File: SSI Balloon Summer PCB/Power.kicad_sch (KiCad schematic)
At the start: 36 parts, among them J1 Battery connector, Q2 DMG2305UX-7, SW1 SW_SPDT, U2 TPS63070RNMR, U3 AP2112K-3.3TRG1, U6 TPS63070RNMR

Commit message: finished footprints for PWR sheet
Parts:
- added D2: BZT52C5V1, Diode_SMD:D_SOD-123, symbol Device:D_Zener
- C1, C10, C19, C9: footprint (none) -> Capacitor_SMD:C_0603_1608Metric
- C15, C16, C17, C18, C2, C20, C21, C22, C3, C4, C5, C6, C7, C8: footprint (none) -> Capacitor_SMD:C_0805_2012Metric
- J1: footprint (none) -> Connector_JST:JST_XH_B2B-XH-A_1x02_P2.50mm_Vertical
- L1, L2: footprint (none) -> Inductor_SMD:L_Coilcraft_XxL4020
- R1, R10, R2, R3, R7, R8: footprint (none) -> Resistor_SMD:R_0603_1608Metric
- R4: value 680k -> AP2112K-3.3TRG1; footprint (none) -> AP2112K-3.3TRG1:SOT95P285X140-5N; Availability (none) -> In Stock; Check_prices (none) -> https://www.snapeda.com/parts/AP2112K-3.3TRG1/Diodes+Inc./v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; MANUFACTURER (none) -> Diodes Inc.; MF (none) -> Diodes Inc.; MP (none) -> AP2112K-3.3TRG1; PARTREV (none) -> 2-2; Package (none) -> SOT-753 Diodes Inc.; Price (none) -> None; SnapEDA_Link (none) -> https://www.snapeda.com/parts/AP2112K-3.3TRG1/Diodes+Inc./v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
- R5: value 130k -> 680k; footprint (none) -> Resistor_SMD:R_0603_1608Metric
- R9: value 412k -> 130k; footprint (none) -> Resistor_SMD:R_0603_1608Metric
- SW1: value SW_SPDT -> 412k; footprint (none) -> Resistor_SMD:R_0603_1608Metric
- U2, U6: value TPS63070RNMR -> SW_SPDT; footprint TPS63070RNMR:VREG_TPS63070RNMR -> Connector_JST:JST_XH_B3B-XH-A_1x03_P2.50mm_Vertical; Availability In Stock -> (none); Check_prices https://www.snapeda.com/parts/TPS63070RNMR/Texas+Instrument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 -> (none); MANUFACTURER Texas Instruments -> (none); MAXIMUM_PACKAGE_HEIGHT 1.0mm -> (none); MF Texas Instruments -> (none); MP TPS63070RNMR -> (none); PARTREV B -> (none); Package VQFN-HR-15 Texas Instruments -> (none); Price None -> (none); STANDARD Manufacturer Recommendations -> (none); SnapEDA_Link https://www.snapeda.com/parts/TPS63070RNMR/Texas+Instrument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 -> (none)
- U3: value AP2112K-3.3TRG1 -> TPS63070RNMR; footprint AP2112K-3.3TRG1:SOT95P285X140-5N -> TPS63070RNMR:VREG_TPS63070RNMR; Check_prices https://www.snapeda.com/parts/AP2112K-3.3TRG1/Diodes+Inc./v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 -> https://www.snapeda.com/parts/TPS63070RNMR/Texas+Instrument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; MANUFACTURER Diodes Inc. -> Texas Instruments; MAXIMUM_PACKAGE_HEIGHT (none) -> 1.0mm; MF Diodes Inc. -> Texas Instruments; MP AP2112K-3.3TRG1 -> TPS63070RNMR; PARTREV 2-2 -> B; Package SOT-753 Diodes Inc. -> VQFN-HR-15 Texas Instruments; STANDARD (none) -> Manufacturer Recommendations; SnapEDA_Link https://www.snapeda.com/parts/AP2112K-3.3TRG1/Diodes+Inc./v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 -> https://www.snapeda.com/parts/TPS63070RNMR/Texas+Instrument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
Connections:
- net VBAT_PROT: now also Q2.2, D2.1 (K); no longer Q2.3
- net at Q2.1, R1.2: now also D2.2 (A)
- net at F1.2: now also Q2.3; no longer Q2.2
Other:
- moved on the sheet: Q2, R1

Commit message: Revised power sheet
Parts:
- removed U2, U6: SW_SPDT, Connector_JST:JST_XH_B3B-XH-A_1x03_P2.50mm_Vertical, symbol TPS63070RNMR:TPS63070RNMR
- added U11, U12: TPS63070RNMR, TPS63070RNMR:VREG_TPS63070RNMR, symbol TPS63070RNMR:TPS63070RNMR
- R4: value AP2112K-3.3TRG1 -> 680k
- R5: value 680k -> 130k
- R9: value 130k -> 412k
- U3: value TPS63070RNMR -> AP2112K-3.3TRG1; footprint TPS63070RNMR:VREG_TPS63070RNMR -> AP2112K-3.3TRG1:SOT95P285X140-5N; Check_prices https://www.snapeda.com/parts/TPS63070RNMR/Texas+Instrument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 -> https://www.snapeda.com/parts/AP2112K-3.3TRG1/Diodes+Inc./v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; MANUFACTURER Texas Instruments -> Diodes Inc.; MAXIMUM_PACKAGE_HEIGHT 1.0mm -> (none); MF Texas Instruments -> Diodes Inc.; MP TPS63070RNMR -> AP2112K-3.3TRG1; PARTREV B -> 2-2; Package VQFN-HR-15 Texas Instruments -> SOT-753 Diodes Inc.; STANDARD Manufacturer Recommendations -> (none); SnapEDA_Link https://www.snapeda.com/parts/TPS63070RNMR/Texas+Instrument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 -> https://www.snapeda.com/parts/AP2112K-3.3TRG1/Diodes+Inc./v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
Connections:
- net +4V1: now also U12.7_8 (VOUT)
- net +5V: now also U11.7_8 (VOUT)
- net GND: now also U11.10 (PGND), U11.15 (VSEL), U11.4 (GND), U12.10 (PGND), U12.15 (VSEL), U12.4 (GND)
- net VBAT_PROT: now also C15.2, C16.2, C17.2, C6.2, C7.2, C8.2, R2.1, R7.1, U11.12_13 (VIN), U12.12_13 (VIN)
- net at R3.1: now also U11.2 (PG)
- net at R8.1: now also U12.2 (PG)
- net at R4.2, R5.1: now also U11.5 (FB)
- net at R10.1, R9.2: now also U12.5 (FB)
- net VBAT: now reaches J1.1 (Pin_1), SW1.2 (B)
- net at R2.2: now also U11.1 (PS/SYNC), U11.14 (EN)
- net at C1.1: now also U11.3 (VAUX)
- net at R7.2: now also U12.1 (PS/SYNC), U12.14 (EN)
- net at L2.1: now also U12.11 (L1)
- net at C19.1: now also U12.3 (VAUX)
- net at L2.2: now also U12.9 (L2)
- net at L1.1: now also U11.11 (L1)
- net at L1.2: now also U11.9 (L2)

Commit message: Layout placement for every sheet except PWR and SD card
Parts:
- J1: now left out of the parts list
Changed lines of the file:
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@@
 	)
 	(junction
-		(at 189.23 45.72)
-		(diameter 0)
-		(color 0 0 0 0)
-	)
-	(junction
 		(at 247.65 128.27)
 		(diameter 0)
@@
 	)
 	(junction
+		(at 189.23 45.72)
+		(diameter 0)
+		(color 0 0 0 0)
+	)
+	(junction
 		(at 120.65 102.87)
 		(diameter 0)
@@
 	(wire
 		(pts
-			(xy 189.23 45.72) (xy 193.04 45.72)
+			(xy 189.23 45.72) (xy 205.74 45.72)
 		)
 		(stroke
@@
 	)
 	(label "VBAT_PROT"
-		(at 193.04 45.72 0)
+		(at 205.74 45.72 0)
 		(effects
 			(font
@@
 		(body_style 1)
 		(exclude_from_sim no)
-		(in_bom yes)
+		(in_bom no)
 		(on_board yes)
 		(in_pos_files yes)

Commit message: Reviewed sensor sheet
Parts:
- J1: now in the parts list
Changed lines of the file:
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@@
 	)
 	(junction
-		(at 247.65 128.27)
+		(at 189.23 45.72)
 		(diameter 0)
 		(color 0 0 0 0)
 	)
 	(junction
-		(at 133.35 93.98)
+		(at 247.65 128.27)
 		(diameter 0)
 		(color 0 0 0 0)
 	)
 	(junction
-		(at 173.99 119.38)
+		(at 133.35 93.98)
 		(diameter 0)
 		(color 0 0 0 0)
 	)
 	(junction
-		(at 233.68 144.78)
+		(at 173.99 119.38)
 		(diameter 0)
 		(color 0 0 0 0)
 	)
 	(junction
-		(at 189.23 45.72)
+		(at 233.68 144.78)
 		(diameter 0)
 		(color 0 0 0 0)
@@
 	)
 	(junction
+		(at 120.65 166.37)
+		(diameter 0)
+		(color 0 0 0 0)
+	)
+	(junction
 		(at 241.3 119.38)
 		(diameter 0)
@@
 	(wire
 		(pts
+			(xy 120.65 166.37) (xy 123.19 166.37)
+		)
+		(stroke
+			(width 0)
+			(type default)
+		)
+	)
+	(wire
+		(pts
 			(xy 43.18 81.28) (xy 43.18 83.82)
 		)
@@
 	(wire
 		(pts
-			(xy 140.97 93.98) (xy 151.13 93.98)
-		)
-		(stroke
-			(width 0)
-			(type default)
-		)
-	)
-	(wire
-		(pts
 			(xy 247.65 128.27) (xy 247.65 130.81)
 		)
@@
 	(wire
 		(pts
-			(xy 189.23 45.72) (xy 205.74 45.72)
+			(xy 189.23 45.72) (xy 193.04 45.72)
 		)
 		(stroke
@@
 	(wire
 		(pts
+			(xy 140.97 93.98) (xy 151.13 93.98)
+		)
+		(stroke
+			(width 0)
+			(type default)
+		)
+	)
+	(wire
+		(pts
 			(xy 120.65 93.98) (xy 120.65 95.25)
 		)
@@
 	(wire
 		(pts
-			(xy 113.03 166.37) (xy 123.19 166.37)
+			(xy 113.03 166.37) (xy 120.65 166.37)
 		)
 		(stroke
@@
 	)
 	(label "VBAT_PROT"
-		(at 205.74 45.72 0)
+		(at 193.04 45.72 0)
 		(effects
 			(font
@@
 		(body_style 1)
 		(exclude_from_sim no)
-		(in_bom no)
+		(in_bom yes)
 		(on_board yes)
 		(in_pos_files yes)
@@
 					(unit 1)
 				)
+			)
+		)
+	)
+	(symbol
+		(lib_id "power:PWR_FLAG")
+		(at 120.65 166.37 180)
+		(unit 1)
+		(body_style 1)
+		(exclude_from_sim no)
+		(in_bom yes)
+		(on_board yes)
+		(in_pos_files yes)
+		(dnp no)
+		(fields_autoplaced yes)
+		(property "Reference" "#FLG06"
+			(at 120.65 168.275 0)
+			(hide yes)
+			(show_name no)
+			(do_not_autoplace no)
+			(effects
+				(font
+					(size 1.27 1.27)
+				)
+			)
+		)
+		(property "Value" "PWR_FLAG"
+			(at 120.65 171.45 0)
+			(show_name no)
+			(do_not_autoplace no)
+			(effects
+				(font
+					(size 1.27 1.27)
+				)
+			)
+		)
+		(property "Footprint" ""
+			(at 120.65 166.37 0)
+			(hide yes)
+			(show_name no)
+			(do_not_autoplace no)
+			(effects
+				(font
+					(size 1.27 1.27)
+				)
+			)
+		)
+		(property "Datasheet" ""
+			(at 120.65 166.37 0)
+			(hide yes)
+			(show_name no)
+			(do_not_autoplace no)
+			(effects
+				(font
+					(size 1.27 1.27)
+				)
+			)
+		)
+		(property "Description" "Special symbol for telling ERC where power comes from"
+			(at 120.65 166.37 0)
+			(hide yes)
+			(show_name no)
+			(do_not_autoplace no)
+			(effects
+				(font
+					(size 1.27 1.27)
+				)
+			)
+		)
+		(pin "1"
+		)
+		(instances
+			(project "SSI Summer Balloons"
+				(path "/3c45a535-6e6b-4825-ad52-82c10cbe7866/1b5737e2-4399-496a-b942-ad94430e2078"
+					(reference "#FLG06")
+					(unit 1)
+				)

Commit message: Reviewed Radio, GPS sheet and minor tweak on power sheet
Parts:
- SW1: value 412k -> SW_SPDT; footprint Resistor_SMD:R_0603_1608Metric -> (none)
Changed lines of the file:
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@@
+	)
+	(symbol
+		(lib_id "Switch:SW_SPDT")
+		(at 129.54 48.26 0)
+		(unit 1)
+		(body_style 1)
+		(exclude_from_sim no)
+		(in_bom yes)
+		(on_board yes)
+		(in_pos_files yes)
+		(dnp no)
+		(fields_autoplaced yes)
+		(property "Reference" "SW1"
+			(at 129.54 39.37 0)
+			(show_name no)
+			(do_not_autoplace no)
+			(effects
+				(font
+					(size 1.27 1.27)
+				)
+			)
+		)
+		(property "Value" "SW_SPDT"
+			(at 129.54 41.91 0)
+			(show_name no)
+			(do_not_autoplace no)
+			(effects
+				(font
+					(size 1.27 1.27)
+				)
+			)
+		)
+		(property "Footprint" ""
+			(at 129.54 48.26 0)
+			(hide yes)
+			(show_name no)
+			(do_not_autoplace no)
+			(effects
+				(font
+					(size 1.27 1.27)
+				)
+			)
+		)
+		(property "Datasheet" ""
+			(at 129.54 55.88 0)
+			(hide yes)
+			(show_name no)
+			(do_not_autoplace no)
+			(effects
+				(font
+					(size 1.27 1.27)
+				)
+			)
+		)
+		(property "Description" "Switch, single pole double throw"
+			(at 129.54 48.26 0)
+			(hide yes)
+			(show_name no)
+			(do_not_autoplace no)
+			(effects
+				(font
+					(size 1.27 1.27)
+				)
+			)
+		)
+		(pin "1"
+		)
+		(pin "3"
+		)
+		(pin "2"
+		)
+		(instances
+			(project "SSI Summer Balloons"
+				(path "/3c45a535-6e6b-4825-ad52-82c10cbe7866/1b5737e2-4399-496a-b942-ad94430e2078"
+					(reference "SW1")
+					(unit 1)
+				)
+			)
+		)
 	)
 	(symbol
@@
 					(unit 1)
 				)
-			)
-		)
-	)
-	(symbol
-		(lib_id "Switch:SW_SPDT")
-		(at 129.54 48.26 0)
-		(unit 1)
-		(body_style 1)
-		(exclude_from_sim no)
-		(in_bom yes)
-		(on_board yes)
-		(in_pos_files yes)
-		(dnp no)
-		(fields_autoplaced yes)
-		(property "Reference" "SW1"
-			(at 129.54 39.37 0)
-			(show_name no)
-			(do_not_autoplace no)
-			(effects
-				(font
-					(size 1.27 1.27)
-				)
-			)
-		)
-		(property "Value" "412k"
-			(at 129.54 41.91 0)
-			(show_name no)
-			(do_not_autoplace no)
-			(effects
-				(font
-					(size 1.27 1.27)
-				)
-			)
-		)
-		(property "Footprint" "Resistor_SMD:R_0603_1608Metric"
-			(at 129.54 48.26 0)
-			(hide yes)
-			(show_name no)
-			(do_not_autoplace no)
-			(effects
-				(font
-					(size 1.27 1.27)
-				)
-			)
-		)
-		(property "Datasheet" ""
-			(at 129.54 55.88 0)
-			(hide yes)
-			(show_name no)
-			(do_not_autoplace no)
-			(effects
-				(font
-					(size 1.27 1.27)
-				)
-			)
-		)
-		(property "Description" "Resistor"
-			(at 129.54 48.26 0)
-			(hide yes)
-			(show_name no)
-			(do_not_autoplace no)
-			(effects
-				(font
-					(size 1.27 1.27)
-				)
-			)
-		)
-		(pin "1"
-		)
-		(pin "2"
-		)
-		(pin "3"
-		)
-		(instances
-			(project "SSI Summer Balloons"
-				(path "/3c45a535-6e6b-4825-ad52-82c10cbe7866/1b5737e2-4399-496a-b942-ad94430e2078"
-					(reference "SW1")
-					(unit 1)
-				)

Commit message: Finished power sheet layout organization
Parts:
- removed R3, R8: 100k, Resistor_SMD:R_0603_1608Metric, symbol Device:R
- C17, C18, C5, C6: footprint Capacitor_SMD:C_0805_2012Metric -> Capacitor_SMD:C_0603_1608Metric
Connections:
- no-connect marks 3 -> 5
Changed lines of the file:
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@@
 	)
 	(junction
-		(at 114.3 93.98)
-		(diameter 0)
-		(color 0 0 0 0)
-	)
-	(junction
 		(at 120.65 93.98)
 		(diameter 0)
@@
 	)
 	(junction
-		(at 241.3 119.38)
-		(diameter 0)
-		(color 0 0 0 0)
-	)
-	(junction
 		(at 62.23 101.6)
 		(diameter 0)
@@
 	)
 	(no_connect
+		(at 227.33 121.92)
+	)
+	(no_connect
 		(at 134.62 50.8)
 	)
 	(no_connect
+		(at 100.33 96.52)
+	)
+	(no_connect
 		(at 227.33 129.54)
 	)
@@
 	(wire
 		(pts
-			(xy 114.3 96.52) (xy 114.3 93.98)
-		)
-		(stroke
-			(width 0)
-			(type default)
-		)
-	)
-	(wire
-		(pts
 			(xy 102.87 101.6) (xy 102.87 102.87)
 		)
@@
 	(wire
 		(pts
-			(xy 102.87 93.98) (xy 114.3 93.98)
-		)
-		(stroke
-			(width 0)
-			(type default)
-		)
-	)
-	(wire
-		(pts
 			(xy 120.65 166.37) (xy 123.19 166.37)
 		)
@@
 	(wire
 		(pts
-			(xy 241.3 119.38) (xy 247.65 119.38)
-		)
-		(stroke
-			(width 0)
-			(type default)
-		)
-	)
-	(wire
-		(pts
 			(xy 158.75 45.72) (xy 167.64 45.72)
 		)
@@
 	(wire
 		(pts
-			(xy 114.3 93.98) (xy 120.65 93.98)
+			(xy 102.87 93.98) (xy 120.65 93.98)
 		)
 		(stroke
@@
 	(wire
 		(pts
-			(xy 241.3 121.92) (xy 241.3 119.38)
-		)
-		(stroke
-			(width 0)
-			(type default)
-		)
-	)
-	(wire
-		(pts
 			(xy 170.18 106.68) (xy 170.18 109.22)
 		)
@@
 	(wire
 		(pts
-			(xy 227.33 121.92) (xy 232.41 121.92)
-		)
-		(stroke
-			(width 0)
-			(type default)
-		)
-	)
-	(wire
-		(pts
 			(xy 60.96 81.28) (xy 60.96 83.82)
 		)
@@
 	(wire
 		(pts
-			(xy 100.33 96.52) (xy 105.41 96.52)
-		)
-		(stroke
-			(width 0)
-			(type default)
-		)
-	)
-	(wire
-		(pts
 			(xy 252.73 116.84) (xy 252.73 119.38)
 		)
@@
 	(wire
 		(pts
-			(xy 229.87 119.38) (xy 241.3 119.38)
+			(xy 229.87 119.38) (xy 247.65 119.38)
 		)
 		(stroke
@@
 	(wire
 		(pts
-			(xy 240.03 121.92) (xy 241.3 121.92)
-		)
-		(stroke
-			(width 0)
-			(type default)
-		)
-	)
-	(wire
-		(pts
 			(xy 43.18 93.98) (xy 46.99 93.98)
 		)
@@
 	)
 	(symbol
-		(lib_id "Device:R")
-		(at 109.22 96.52 90)
-		(unit 1)
-		(body_style 1)
-		(exclude_from_sim no)
-		(in_bom yes)
-		(on_board yes)
-		(in_pos_files yes)
-		(dnp no)
-		(property "Reference" "R3"
-			(at 105.918 98.806 90)
-			(show_name no)
-			(do_not_autoplace no)
-			(effects
-				(font
-					(size 1.27 1.27)
-				)
-			)
-		)
-		(property "Value" "100k"
-			(at 110.236 98.806 90)
-			(show_name no)
-			(do_not_autoplace no)
-			(effects
-				(font
-					(size 1.27 1.27)
-				)
-			)
-		)
-		(property "Footprint" "Resistor_SMD:R_0603_1608Metric"
-			(at 109.22 98.298 90)
-			(hide yes)
-			(show_name no)
-			(do_not_autoplace no)
-			(effects
-				(font
-					(size 1.27 1.27)
-				)
-			)
-		)
-		(property "Datasheet" ""
-			(at 109.22 96.52 0)
-			(hide yes)
-			(show_name no)
-			(do_not_autoplace no)
-			(effects
-				(font
-					(size 1.27 1.27)
-				)
-			)
-		)
-		(property "Description" "Resistor"
-			(at 109.22 96.52 0)
-			(hide yes)
-			(show_name no)
-			(do_not_autoplace no)
-			(effects
-				(font
-					(size 1.27 1.27)
-				)
-			)
-		)
-		(pin "1"
-		)
-		(pin "2"
-		)
-		(instances
-			(project "SSI Summer Balloons"
-				(path "/3c45a535-6e6b-4825-ad52-82c10cbe7866/1b5737e2-4399-496a-b942-ad94430e2078"
-					(reference "R3")
-					(unit 1)
-				)
-			)
-		)
-	)
-	(symbol
 		(lib_id "power:GND")
 		(at 125.73 81.28 180)
@@
 			)
 		)
-		(property "Footprint" "Capacitor_SMD:C_0805_2012Metric"
+		(property "Footprint" "Capacitor_SMD:C_0603_1608Metric"
 			(at 61.9252 91.44 0)
 			(hide yes)
@@
 	)
 	(symbol
-		(lib_id "Device:R")
-		(at 236.22 121.92 90)
-		(unit 1)
-		(body_style 1)
-		(exclude_from_sim no)
-		(in_bom yes)
-		(on_board yes)
-		(in_pos_files yes)
-		(dnp no)
-		(property "Reference" "R8"
-			(at 232.918 124.206 90)
-			(show_name no)
-			(do_not_autoplace no)
-			(effects
-				(font
-					(size 1.27 1.27)
-				)
-			)
-		)
-		(property "Value" "100k"
-			(at 237.236 124.206 90)
-			(show_name no)
-			(do_not_autoplace no)
-			(effects
-				(font
-					(size 1.27 1.27)
-				)
-			)
-		)
-		(property "Footprint" "Resistor_SMD:R_0603_1608Metric"
-			(at 236.22 123.698 90)
-			(hide yes)
-			(show_name no)
-			(do_not_autoplace no)
-			(effects
-				(font
-					(size 1.27 1.27)
-				)
-			)
-		)
-		(property "Datasheet" ""
-			(at 236.22 121.92 0)
-			(hide yes)
-			(show_name no)
-			(do_not_autoplace no)
-			(effects
-				(font
-					(size 1.27 1.27)
-				)
-			)
-		)
-		(property "Description" "Resistor"
-			(at 236.22 121.92 0)
-			(hide yes)
-			(show_name no)
-			(do_not_autoplace no)
-			(effects
-				(font
-					(size 1.27 1.27)
-				)
-			)
-		)
-		(pin "1"
-		)
-		(pin "2"
-		)
-		(instances
-			(project "SSI Summer Balloons"
-				(path "/3c45a535-6e6b-4825-ad52-82c10cbe7866/1b5737e2-4399-496a-b942-ad94430e2078"
-					(reference "R8")
-					(unit 1)
-				)
-			)
-		)
-	)
-	(symbol
 		(lib_id "Device:C")
 		(at 229.87 113.03 0)
@@
 			)
 		)
-		(property "Footprint" "Capacitor_SMD:C_0805_2012Metric"
+		(property "Footprint" "Capacitor_SMD:C_0603_1608Metric"
 			(at 230.8352 116.84 0)
 			(hide yes)
@@
 			)
 		)
-		(property "Footprint" "Capacitor_SMD:C_0805_2012Metric"
+		(property "Footprint" "Capacitor_SMD:C_0603_1608Metric"
 			(at 188.9252 116.84 0)
 			(hide yes)
@@
 			)
 		)
-		(property "Footprint" "Capacitor_SMD:C_0805_2012Metric"
+		(property "Footprint" "Capacitor_SMD:C_0603_1608Metric"
 			(at 103.8352 91.44 0)
 			(hide yes)

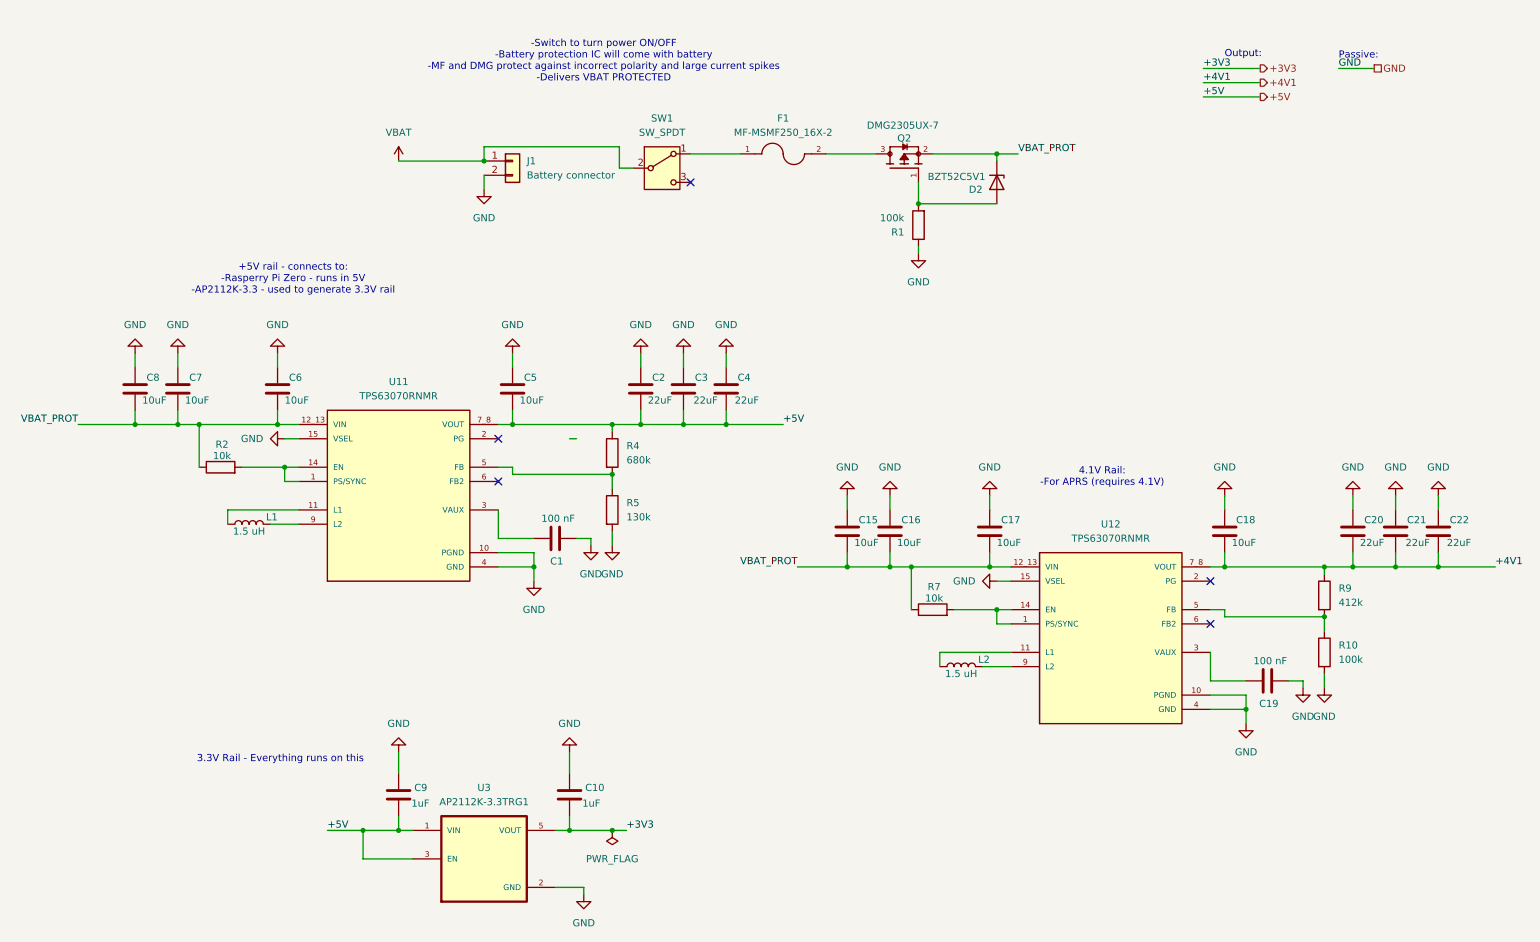
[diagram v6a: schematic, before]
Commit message: Overhauled power symbols for consistency and ERC
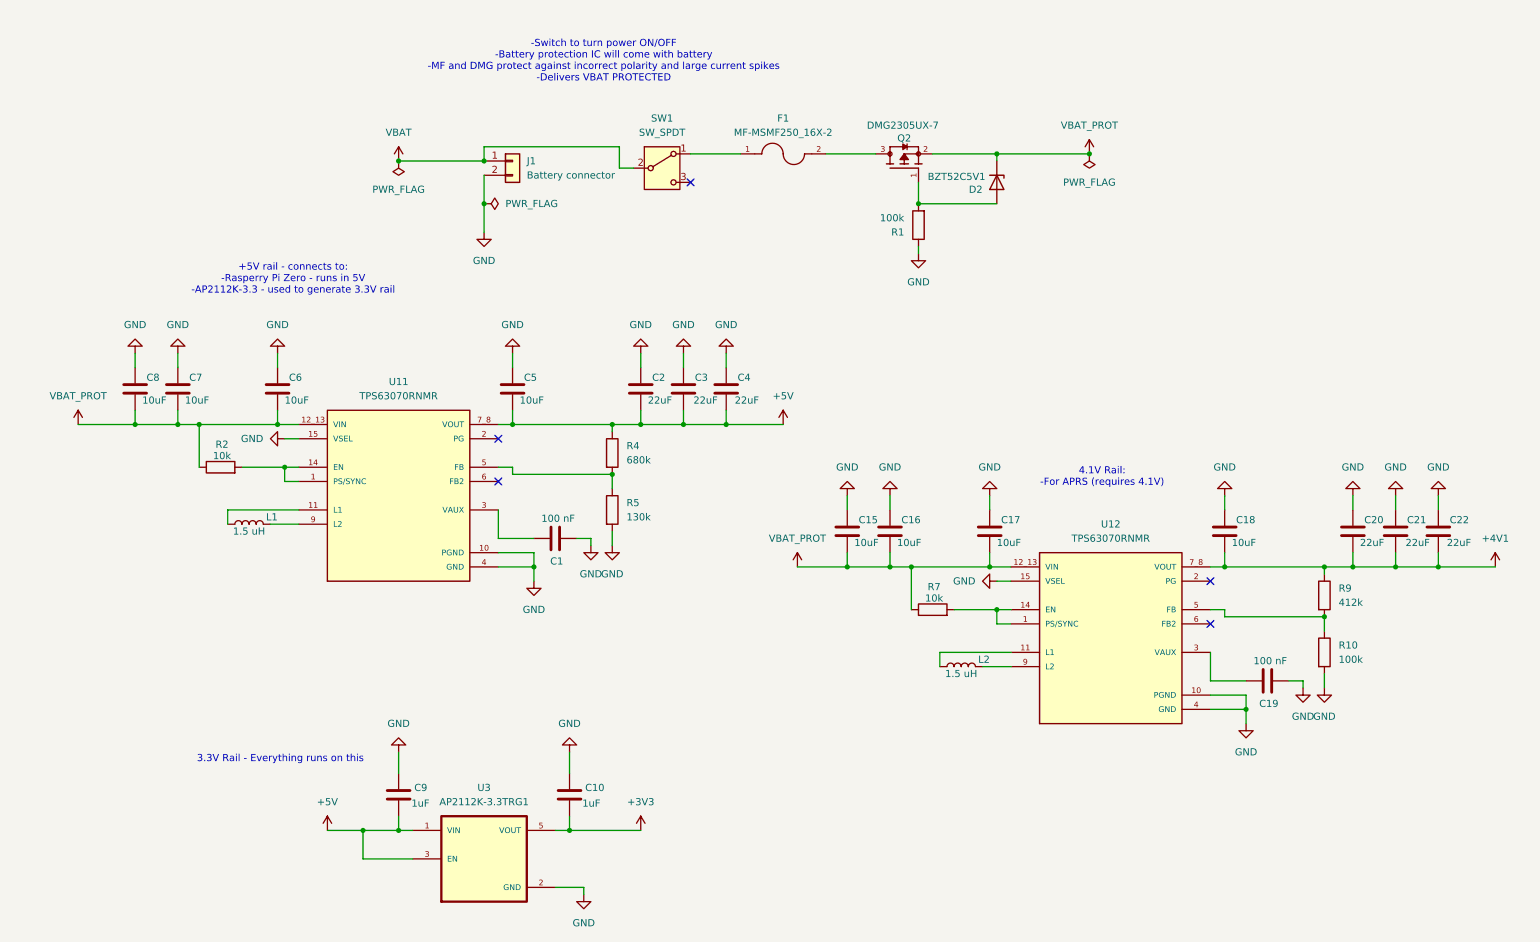
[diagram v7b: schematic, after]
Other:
- note removed: "Output:"
- note removed: "Passive:"
